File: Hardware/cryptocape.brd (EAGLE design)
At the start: 86.4 x 54.6 mm, 50 parts, among them J1 AVR_SPI_PRG_6PTH, U2 ATMEGA328P, U3 EEPROM-I2CSMD, Y1 16MHz

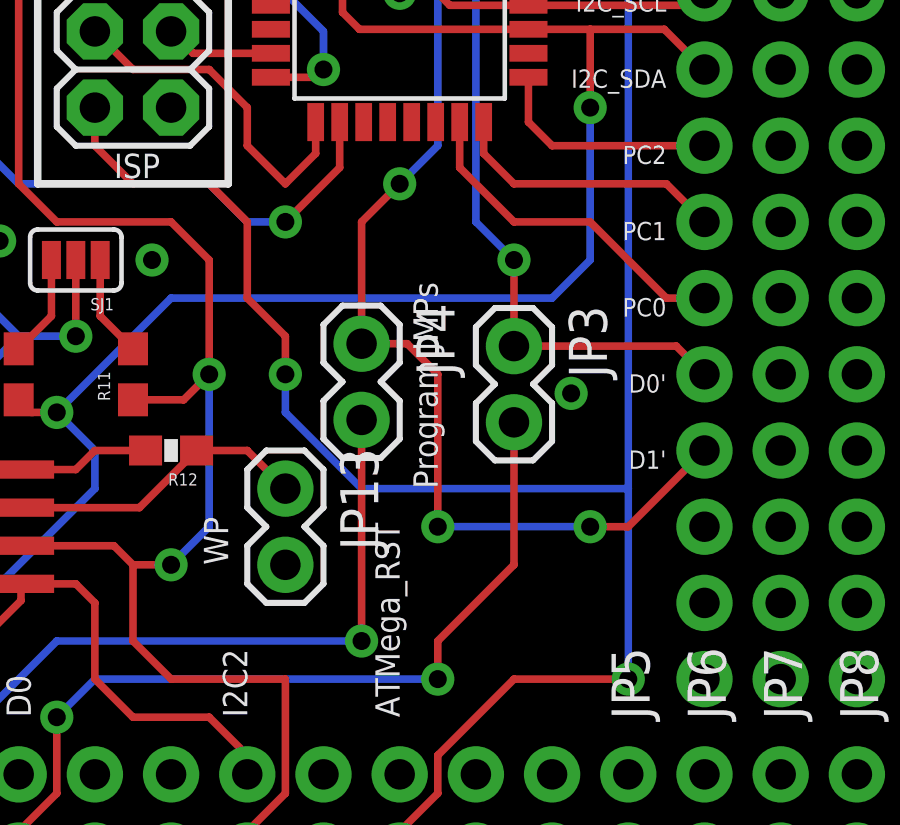
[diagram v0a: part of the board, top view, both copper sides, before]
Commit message: Fixes spacing and silk for jumpers
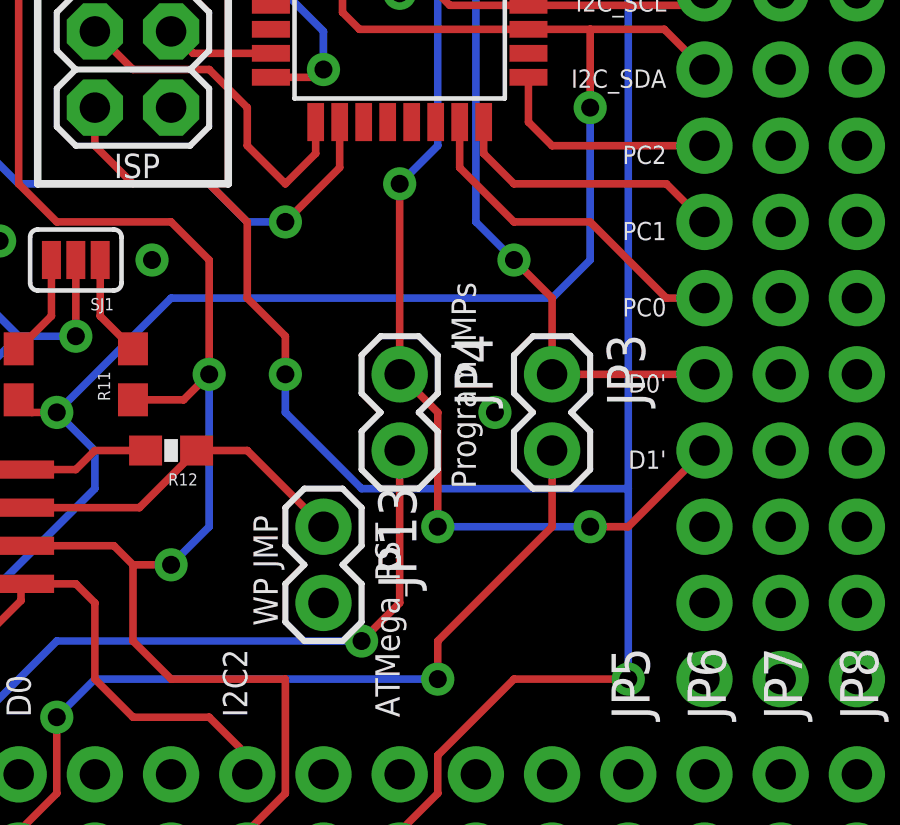
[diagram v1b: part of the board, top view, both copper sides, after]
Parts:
- moved JP13 1.80 mm to (45.7, 12.7)
- moved JP4 1.63 mm to (48.3, 17.8)
- moved JP3 1.58 mm to (53.3, 17.8)
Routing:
- net D1': track 35.3 -> 33.4 mm
- net N$1: track 10.1 -> 11.9 mm
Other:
- board text added: "WP JMP"
- board text removed: "WP"
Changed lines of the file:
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@@
 <setting verticaltext="up"/>
 </settings>
-<grid distance="0.05" unitdist="inch" unit="inch" style="lines" multiple="1" display="yes" altdistance="0.005" altunitdist="inch" altunit="inch"/>
+<grid distance="0.1" unitdist="inch" unit="inch" style="lines" multiple="1" display="yes" altdistance="0.005" altunitdist="inch" altunit="inch"/>
 <layers>
 <layer number="1" name="Top" color="4" fill="1" visible="yes" active="yes"/>
@@
 <text x="43.18" y="6.35" size="0.8128" layer="22" font="vector" ratio="15" rot="SMR270" align="bottom-right">I2C2</text>
 <text x="48.26" y="6.35" size="0.8128" layer="22" font="vector" ratio="15" rot="SMR270" align="bottom-right">ATMega_RST</text>
-<text x="49.53" y="13.97" size="0.8128" layer="21" font="vector" ratio="15" rot="R90">Program JMPs</text>
+<text x="50.8" y="13.97" size="0.8128" layer="21" font="vector" ratio="15" rot="R90">Program JMPs</text>
 <wire x1="36.195" y1="33.02" x2="36.195" y2="24.13" width="0.254" layer="21"/>
 <wire x1="36.195" y1="24.13" x2="42.545" y2="24.13" width="0.254" layer="21"/>
@@
 <text x="57.15" y="43.18" size="0.762" layer="22" font="vector" ratio="15" rot="SMR0" align="top-left">3.3V</text>
 <text x="38.735" y="24.3205" size="0.8128" layer="22" font="vector" ratio="15" rot="SMR0" align="bottom-right">ISP</text>
-<text x="49.53" y="13.97" size="0.8128" layer="22" font="vector" ratio="15" rot="SMR270" align="bottom-right">Program JMPs</text>
+<text x="50.8" y="13.97" size="0.8128" layer="22" font="vector" ratio="15" rot="SMR270" align="bottom-right">Program JMPs</text>
 <text x="83.82" y="7.62" size="4.318" layer="22" font="vector" ratio="15" rot="SMR270" align="bottom-right">CryptoCape</text>
 <text x="14.605" y="19.05" size="0.8128" layer="21" font="vector" ratio="15">32KHZ</text>
@@
 <text x="57.15" y="20.32" size="0.6096" layer="22" font="vector" ratio="15" rot="SMR0" align="top-left">PC0</text>
 <text x="57.15" y="20.32" size="0.6096" layer="21" font="vector" ratio="15" rot="R180">PC0</text>
-<text x="42.545" y="11.43" size="0.8128" layer="21" font="vector" ratio="15" rot="R90">WP</text>
-<text x="42.545" y="11.43" size="0.8128" layer="22" font="vector" ratio="15" rot="SMR270" align="bottom-right">WP</text>
+<text x="44.196" y="9.398" size="0.8128" layer="21" font="vector" ratio="15" rot="R90">WP JMP</text>
+<text x="44.196" y="9.398" size="0.8128" layer="22" font="vector" ratio="15" rot="SMR270" align="bottom-right">WP JMP</text>
 <text x="14.605" y="12.7" size="0.8128" layer="22" font="vector" ratio="15" rot="SMR180" align="top-left">SQW/INT</text>
 <text x="14.605" y="12.7" size="0.8128" layer="21" font="vector" ratio="15">SQW/INT</text>
@@
 </element>
 <element name="BAT1" library="SparkFun-Electromechanical" package="BATTCON_12MM" value="3V" x="6.858" y="10.795" rot="R90"/>
-<element name="JP3" library="SparkFun-Passives" package="1X02" value="Serial Program JMP" x="52.07" y="18.72" rot="R270"/>
-<element name="JP4" library="SparkFun-Passives" package="1X02" value="Serial Program JMP" x="46.99" y="18.8" rot="R270"/>
+<element name="JP3" library="SparkFun-Passives" package="1X02" value="Serial Program JMP" x="53.34" y="17.78" rot="R270"/>
+<element name="JP4" library="SparkFun-Passives" package="1X02" value="Serial Program JMP" x="48.26" y="17.78" rot="R270"/>
 <element name="C3" library="SparkFun-Capacitors" package="0603-CAP" value="0.1uF" x="20.32" y="11.43" rot="R180">
 <attribute name="PROD_ID" value="CAP-00810" x="20.32" y="11.43" size="1.778" layer="27" rot="R180" display="off"/>
@@
 <element name="U$4" library="SparkFun-Aesthetics" package="SFE_LOGO_NAME_FLAME_.1" value="" x="43.18" y="43.18"/>
 <element name="U$5" library="SparkFun-Aesthetics" package="SFE_LOGO_NAME_FLAME_.1" value="" x="54.61" y="43.18" rot="SMR0"/>
-<element name="JP13" library="SparkFun-Passives" package="1X02" value="Jump for Read/Write" x="44.45" y="13.97" rot="R270"/>
+<element name="JP13" library="SparkFun-Passives" package="1X02" value="Jump for Read/Write" x="45.72" y="12.7" rot="R270"/>
 <element name="JP14" library="SparkFun-Passives" package="1X02" value="" x="12.7" y="19.05" rot="R270"/>
 <element name="U$6" library="SparkFun-Aesthetics" package="OSHW-LOGO-S" value="" x="16.51" y="8.89" rot="MR0"/>
@@
 <via x="20.955" y="13.335" extent="1-16" drill="0.6"/>
 <via x="54.61" y="35.56" extent="1-16" drill="0.6"/>
-<via x="53.975" y="17.145" extent="1-16" drill="0.6"/>
+<via x="51.435" y="16.51" extent="1-16" drill="0.6"/>
 </signal>
 <signal name="RST">
@@
 <via x="49.53" y="7.62" extent="1-16" drill="0.6"/>
 <wire x1="49.53" y1="7.62" x2="49.53" y2="8.89" width="0.254" layer="1"/>
-<wire x1="49.53" y1="8.89" x2="52.07" y2="11.43" width="0.254" layer="1"/>
-<wire x1="52.07" y1="11.43" x2="52.07" y2="16.18" width="0.254" layer="1"/>
+<wire x1="49.53" y1="8.89" x2="53.34" y2="12.7" width="0.254" layer="1"/>
+<wire x1="53.34" y1="12.7" x2="53.34" y2="15.24" width="0.254" layer="1"/>
 </signal>
 <signal name="D1">
@@
 <wire x1="36.83" y1="8.89" x2="46.99" y2="8.89" width="0.254" layer="16"/>
 <via x="46.99" y="8.89" extent="1-16" drill="0.6"/>
-<wire x1="46.99" y1="8.89" x2="46.99" y2="16.26" width="0.254" layer="1"/>
+<wire x1="46.99" y1="8.89" x2="48.26" y2="10.16" width="0.254" layer="1"/>
+<wire x1="48.26" y1="10.16" x2="48.26" y2="15.24" width="0.254" layer="1"/>
 </signal>
 <signal name="AT328P_RST">
@@
 <wire x1="51.365" y1="31.68" x2="50.8" y2="31.115" width="0.254" layer="1"/>
 <wire x1="52.5526" y1="31.68" x2="51.365" y2="31.68" width="0.254" layer="1"/>
-<wire x1="52.07" y1="18.72" x2="52.07" y2="21.59" width="0.254" layer="1"/>
 <contactref element="JP5" pad="5"/>
-<wire x1="52.07" y1="18.72" x2="57.48" y2="18.72" width="0.254" layer="1"/>
-<wire x1="57.48" y1="18.72" x2="58.42" y2="17.78" width="0.254" layer="1"/>
 <wire x1="50.8" y1="22.86" x2="52.07" y2="21.59" width="0.254" layer="16"/>
+<wire x1="53.34" y1="17.78" x2="58.42" y2="17.78" width="0.254" layer="1"/>
+<wire x1="53.34" y1="17.78" x2="53.34" y2="20.32" width="0.254" layer="1"/>
+<wire x1="53.34" y1="20.32" x2="52.07" y2="21.59" width="0.254" layer="1"/>
 </signal>
 <signal name="D1'">
@@
 <wire x1="49.53" y1="25.4" x2="48.26" y2="24.13" width="0.254" layer="16"/>
 <via x="48.26" y="24.13" extent="1-16" drill="0.6"/>
-<wire x1="48.26" y1="24.13" x2="46.99" y2="22.86" width="0.254" layer="1"/>
-<wire x1="46.99" y1="18.8" x2="46.99" y2="22.86" width="0.254" layer="1"/>
 <contactref element="JP5" pad="4"/>
-<wire x1="46.99" y1="18.8" x2="48.51" y2="18.8" width="0.254" layer="1"/>
-<wire x1="48.51" y1="18.8" x2="49.53" y2="17.78" width="0.254" layer="1"/>
-<wire x1="49.53" y1="17.78" x2="49.53" y2="12.7" width="0.254" layer="1"/>
 <via x="49.53" y="12.7" extent="1-16" drill="0.6"/>
 <wire x1="49.53" y1="12.7" x2="54.61" y2="12.7" width="0.254" layer="16"/>
@@
 <wire x1="54.61" y1="12.7" x2="55.88" y2="12.7" width="0.254" layer="1"/>
 <wire x1="55.88" y1="12.7" x2="58.42" y2="15.24" width="0.254" layer="1"/>
+<wire x1="49.53" y1="12.7" x2="49.53" y2="16.51" width="0.254" layer="1"/>
+<wire x1="49.53" y1="16.51" x2="48.26" y2="17.78" width="0.254" layer="1"/>
+<wire x1="48.26" y1="17.78" x2="48.26" y2="24.13" width="0.254" layer="1"/>
 </signal>
 <signal name="MOSI">
@@
 <wire x1="39.585" y1="13.335" x2="41.49" y2="15.24" width="0.254" layer="1"/>
 <wire x1="41.49" y1="15.24" x2="43.18" y2="15.24" width="0.254" layer="1"/>
-<wire x1="43.18" y1="15.24" x2="44.45" y2="13.97" width="0.254" layer="1"/>
+<wire x1="43.18" y1="15.24" x2="45.72" y2="12.7" width="0.254" layer="1"/>
 </signal>
 <signal name="PD2">

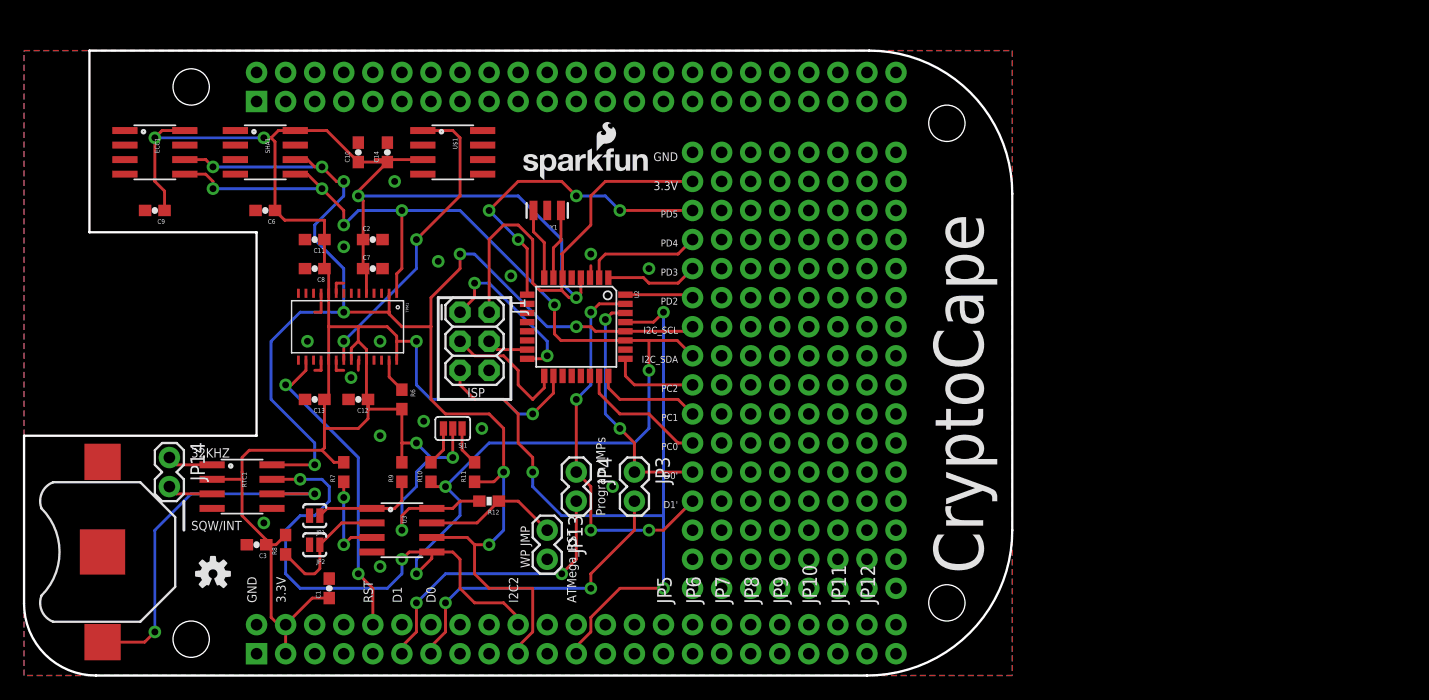
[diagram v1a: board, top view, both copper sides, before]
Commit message: tightening up footprints, still a work in progress
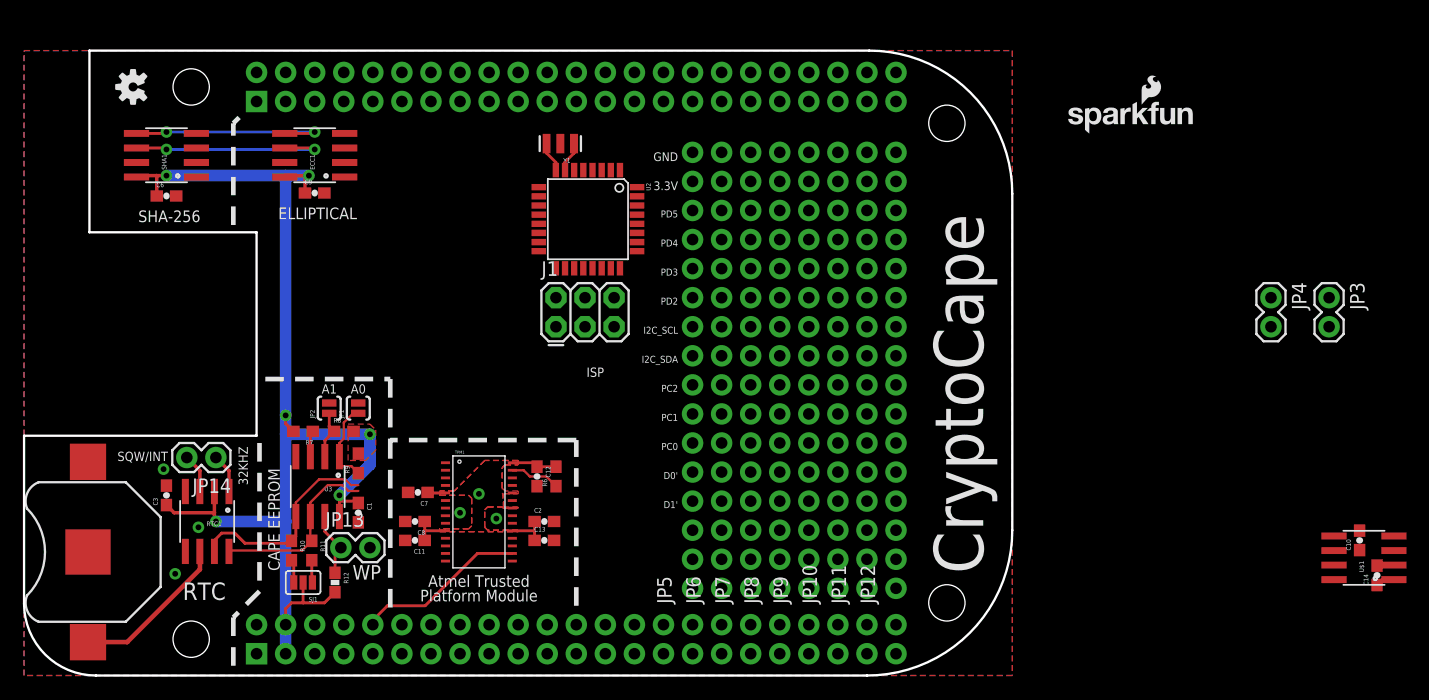
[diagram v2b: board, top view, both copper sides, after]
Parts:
- moved C14 94.1 mm to (118.2, 8.76)
- moved C10 93.8 mm to (116.7, 11.8)
- moved U$1 87.2 mm to (117.1, 10.3), turned to 90 degrees
- moved JP3 62.6 mm to (114.0, 33.0)
- moved JP4 62.6 mm to (109.0, 33.0)
- moved U$5 48.2 mm to (102.6, 47.2)
- moved U$4 47.8 mm to (90.8, 47.2)
- moved U$3 43.1 mm to (9.53, 51.4), turned to 90 degrees
- moved U$6 43.1 mm to (9.53, 51.4), turned to 270 degrees
- moved C2 28.8 mm to (45.5, 13.5)
- moved C11 27.7 mm to (34.2, 11.8)
- moved C8 23.8 mm to (34.2, 13.5)
- moved C13 23.5 mm to (45.5, 11.8), turned to 0 degrees
- moved TPM1 20.3 mm to (39.8, 14.0), turned to 0 degrees
- moved C7 20.0 mm to (34.4, 16.0), turned to 180 degrees
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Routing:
- net 3.3V: track 259.8 -> 115.9 mm, vias 9 -> 7
- net I2C2_SDA: track 148.7 -> 36.7 mm, vias 10 -> 2
- net I2C2_SCL: track 141.9 -> 34.3 mm, vias 9 -> 2
- net AT328P_RST: track 65.7 -> 0.00 mm, vias 3 -> 0
- net D1': track 33.4 -> 0.00 mm, vias 4 -> 0
- net PD5: track 28.6 -> 0.00 mm, vias 4 -> 0
- net D0: track 27.4 -> 0.00 mm, vias 2 -> 0
- net TPM_CLK: track 27.2 -> 0.00 mm, vias 2 -> 0
- net D1: track 25.6 -> 0.00 mm, vias 2 -> 0
- net D0': track 21.5 -> 0.00 mm, vias 2 -> 0
- net VBAT: track 32.8 -> 14.0 mm, vias 2 -> 0
- net MISO: track 14.7 -> 0.00 mm, vias 2 -> 0
- net SYS_RESET: track 27.3 -> 15.0 mm, vias 2 -> 0
- net SCK: track 11.7 -> 0.00 mm
- net PC0: track 11.5 -> 0.00 mm
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- added copper zone on layer 1, net 3.3V
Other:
- board text added: "A0"
- board text added: "A1"
- board text added: "Atmel Trusted"
- board text added: "CAPE EEPROM"
- board text added: "ELLIPTICAL"
- board text added: "Platform Module"
- board text added: "RTC"
- board text added: "SHA-256"
- board text added: "WP"
- board text removed: "ATMega_RST"
- board text removed: "D0"
- board text removed: "D1"
- board text removed: "I2C2"
- board text removed: "Program JMPs"
- board text removed: "RST"
- board text removed: "WP JMP"
